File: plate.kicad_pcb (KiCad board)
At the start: 2 copper layers, 151.2 x 102.5 mm, 5 parts, among them M2 MountingHole_2.2mm_M2

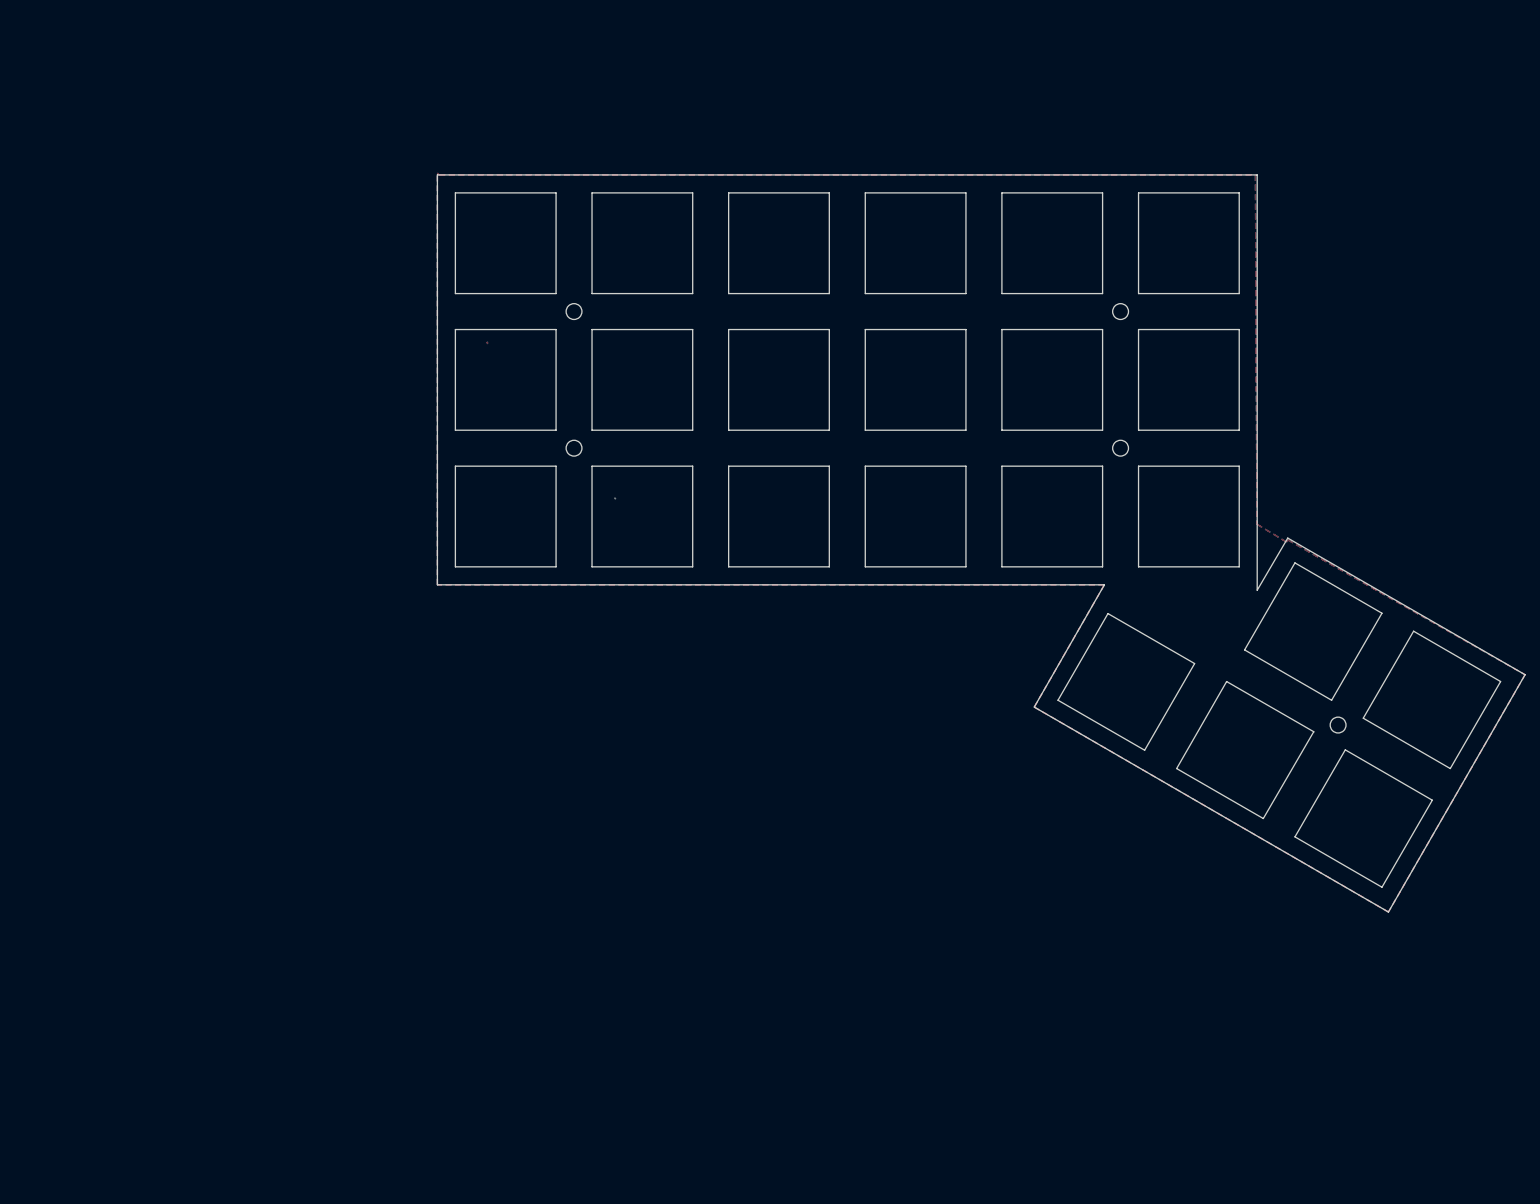
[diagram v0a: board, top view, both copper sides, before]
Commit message: Add case base to plate PCB
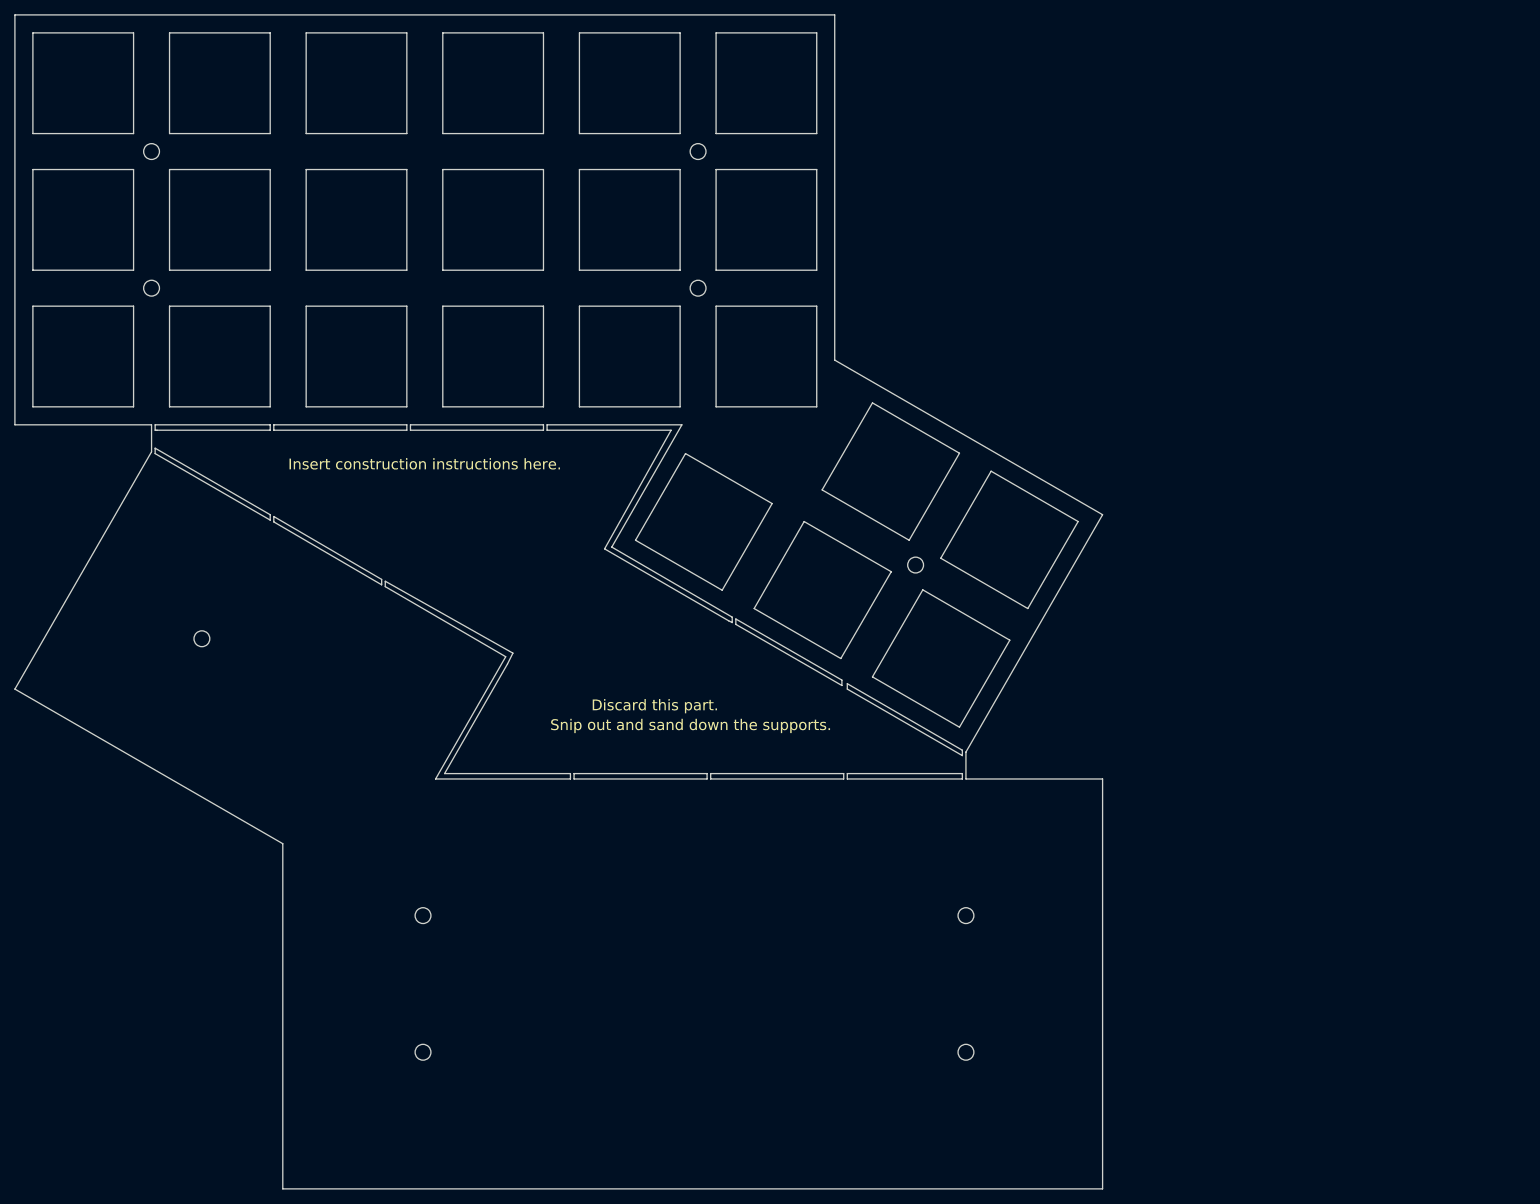
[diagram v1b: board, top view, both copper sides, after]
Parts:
- added M2: MountingHole_2.2mm_M2, Mounting_Holes:MountingHole_2.2mm_M2, F.Cu at (153.0, 151.5)
- added M2: MountingHole_2.2mm_M2, Mounting_Holes:MountingHole_2.2mm_M2, F.Cu at (77.5, 151.5)
- added M2: MountingHole_2.2mm_M2, Mounting_Holes:MountingHole_2.2mm_M2, F.Cu at (153.0, 170.5)
- added M2: MountingHole_2.2mm_M2, Mounting_Holes:MountingHole_2.2mm_M2, F.Cu at (77.5, 170.5)
- added M2: MountingHole_2.2mm_M2, Mounting_Holes:MountingHole_2.2mm_M2, F.Cu at (46.8, 113.0)
- moved M2 62.8 mm to (39.8, 64.2)
- moved M2 62.8 mm to (146.0, 102.8)
- moved M2 62.8 mm to (115.8, 45.2)
- moved M2 62.8 mm to (39.8, 45.2)
- moved M2 62.8 mm to (115.8, 64.2)
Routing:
- removed copper zone on B.Cu, net GND
- removed copper zone on F.Cu, net GND
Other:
- board size 151.2 x 102.5 mm -> 151.2 x 163.2 mm
- board text added: "Discard this part."
- board text added: "Insert construction instructions here."
- board text added: "Snip out and sand down the supports."
